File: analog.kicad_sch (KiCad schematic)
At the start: 13 parts, among them U3 AD620, U4 OPA358, U5 OPA358

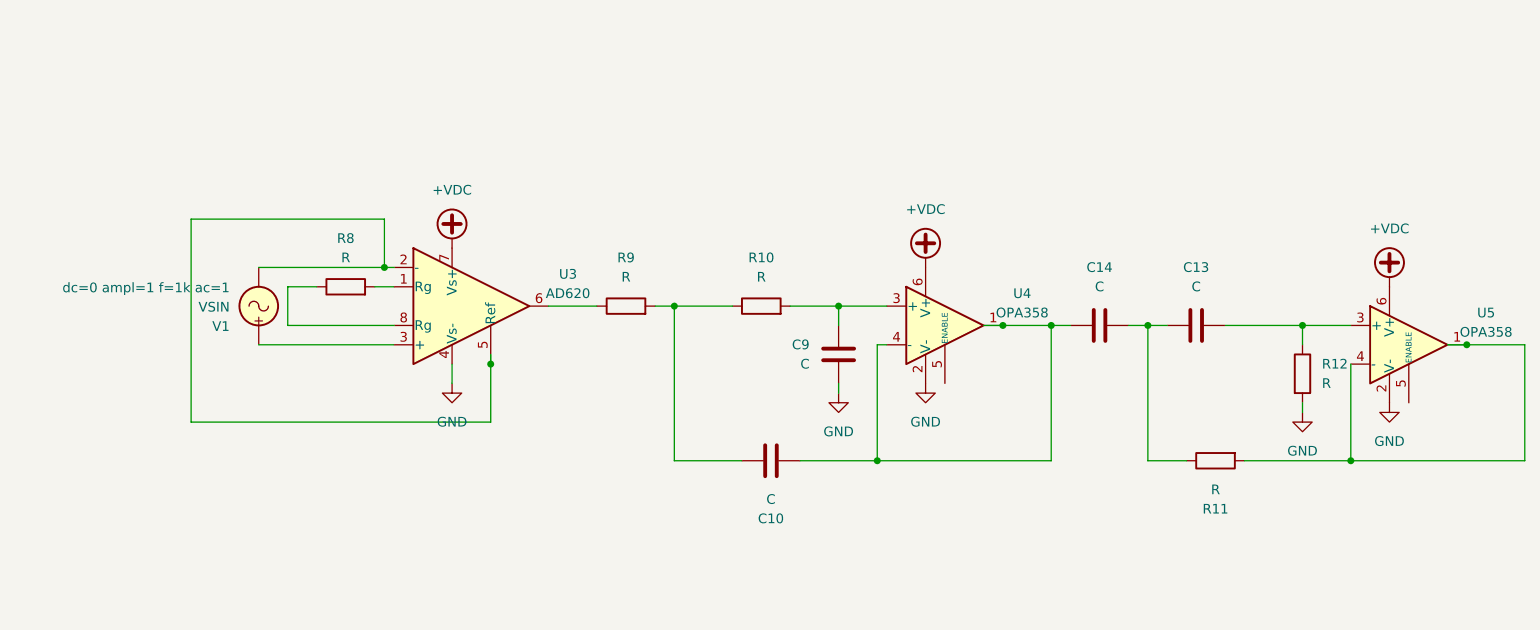
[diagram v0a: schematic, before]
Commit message: removed high pass
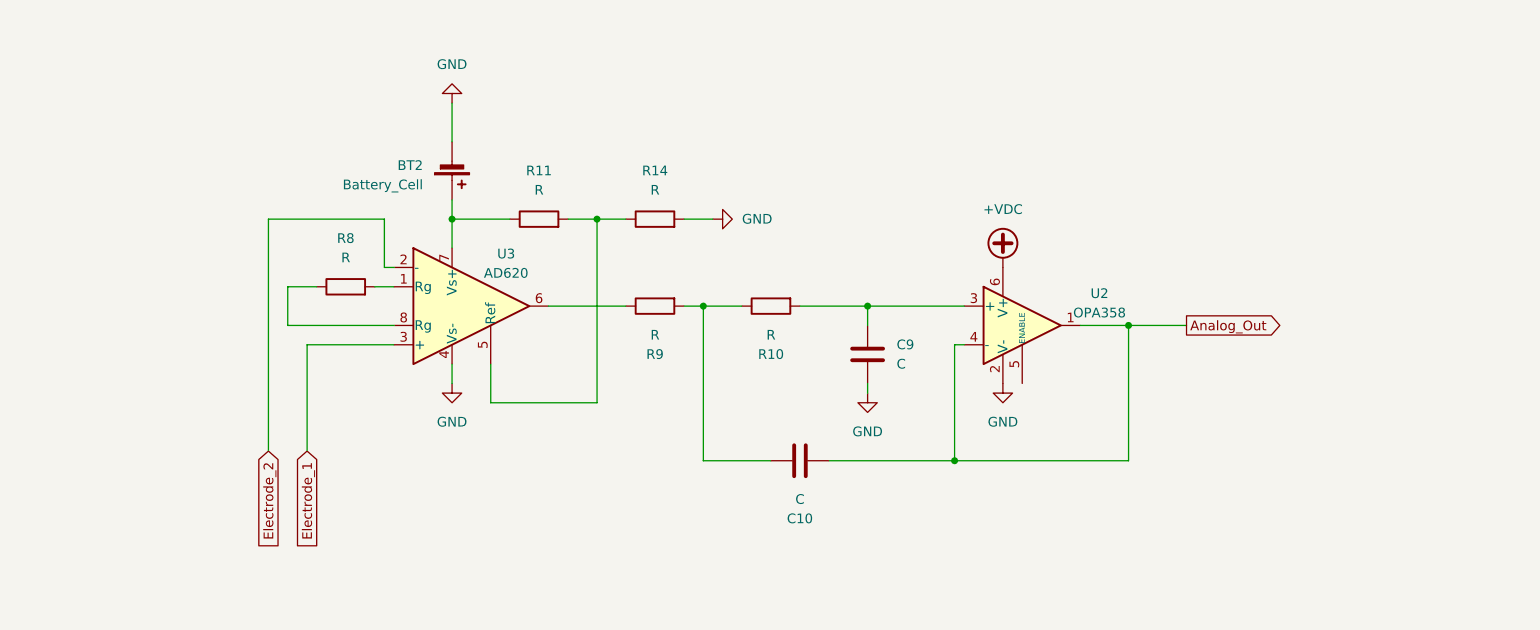
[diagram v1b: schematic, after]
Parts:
- removed C13, C14: C, symbol Device:C
- removed R12: R, symbol Device:R
- removed U4, U5: OPA358, symbol OPA358:OPA358
- removed V1: VSIN, symbol Simulation_SPICE:VSIN
- added BT2: Battery_Cell, symbol Device:Battery_Cell
- added R14: R, symbol Device:R
- added U2: OPA358, opa358-local:DCK6-M, symbol OPA358:OPA358
- U3: footprint (none) -> ad620-local:R_8_ADI-M
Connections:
- net +VDC: now also U2.6 (V+); no longer U3.7 (Vs+)
- net GND: now also BT2.2 (-), R14.2, U2.2 (V-)
- net at R11.1: now also U3.7 (Vs+), BT2.1 (+)
- net at C9.1, R10.2: now also U2.3 (+)
- net at R11.2: now also U3.5 (Ref), R14.1
- net Analog_Out: now reaches C10.2
- net Analog_Out: now also U2.1, U2.4 (-)
- net Electrode_2: now reaches U3.2 (-)
- net Electrode_2: no longer U3.5 (Ref)
- net Electrode_1: now reaches U3.3 (+)
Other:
- moved on the sheet: C10, C9, R10, R9

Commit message: Modified analog as per sir(Lab)
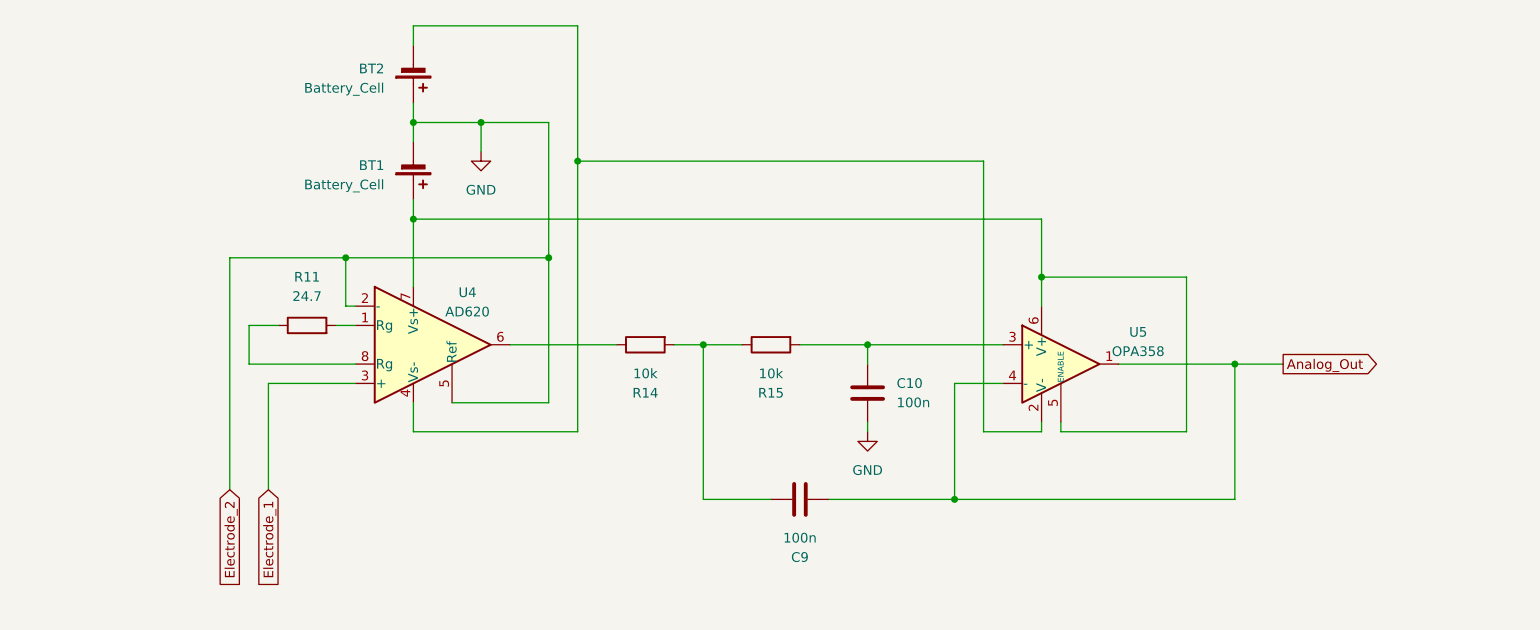
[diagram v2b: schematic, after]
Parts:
- removed R10, R8, R9: R, symbol Device:R
- removed U2: OPA358, opa358-local:DCK6-M, symbol OPA358:OPA358
- removed U3: AD620, ad620-local:R_8_ADI-M, symbol Amplifier_Instrumentation:AD620
- added BT1: Battery_Cell, symbol Device:Battery_Cell
- added R15: 10k, symbol Device:R
- added U4: AD620, ad620-local:R_8_ADI-M, symbol Amplifier_Instrumentation:AD620
- added U5: OPA358, opa358-local:DCK6-M, symbol OPA358:OPA358
- C10, C9: value C -> 100n
- R11: value R -> 24.7
- R14: value R -> 10k
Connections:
- net Analog_Out: now also C9.2, U5.1, U5.4 (-); no longer C10.2
- net Electrode_1: now also U4.3 (+)
- net GND: now also BT2.1 (+), C10.2, BT1.2 (-), U4.2 (-), U4.5 (Ref); no longer BT2.2 (-), C9.2, R14.2
- net at C9.1: now also R14.2, R15.1
- net at R11.1: now also U4.8 (Rg); no longer BT2.1 (+)
- net at R11.2: now also U4.1 (Rg); no longer R14.1
- net at C10.1: now also R15.2, U5.3 (+)
- new net: BT2.2 (-), U4.4 (Vs-), U5.2 (V-)
- new net: BT1.1 (+), U4.7 (Vs+), U5.5 (ENABLE), U5.6 (V+)
- new net: R14.1, U4.6

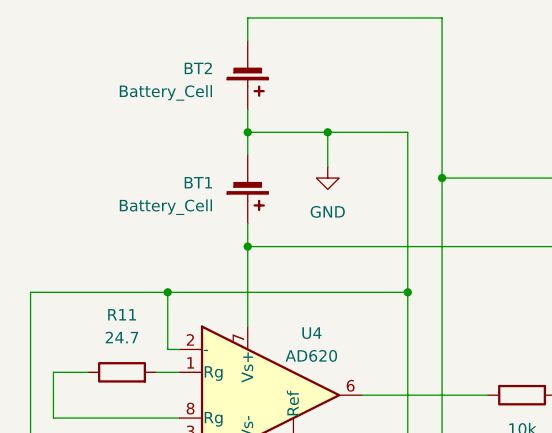
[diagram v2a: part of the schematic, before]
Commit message: Created and added Symbols for previous blackboxes
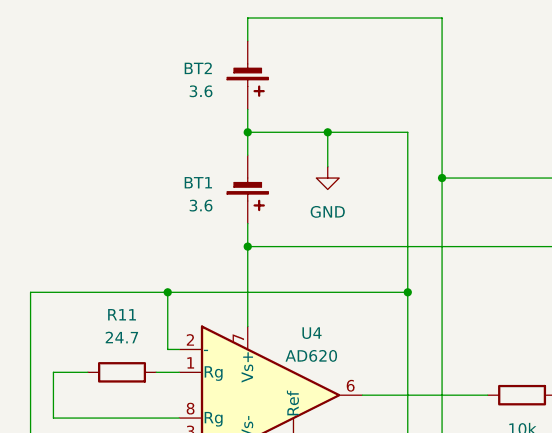
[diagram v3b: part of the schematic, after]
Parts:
- BT1, BT2: value Battery_Cell -> 3.6

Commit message: Assigned footprints for Resistors and Capacitors
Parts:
- C10, C9: footprint (none) -> Capacitor_SMD:C_0201_0603Metric
- R11, R14, R15: footprint (none) -> Resistor_SMD:R_0201_0603Metric
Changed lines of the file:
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@@
 			)
 		)
-		(property "Footprint" ""
+		(property "Footprint" "Capacitor_SMD:C_0201_0603Metric"
 			(at 150.8252 100.33 0)
 			(effects
@@
 			)
 		)
-		(property "Footprint" ""
+		(property "Footprint" "Resistor_SMD:R_0201_0603Metric"
 			(at 137.16 88.392 90)
 			(effects
@@
 			)
 		)
-		(property "Footprint" ""
+		(property "Footprint" "Resistor_SMD:R_0201_0603Metric"
 			(at 76.2 89.408 90)
 			(effects
@@
 			)
 		)
-		(property "Footprint" ""
+		(property "Footprint" "Resistor_SMD:R_0201_0603Metric"
 			(at 120.65 88.392 90)
 			(effects
@@
 			)
 		)
-		(property "Footprint" ""
+		(property "Footprint" "Capacitor_SMD:C_0201_0603Metric"
 			(at 144.78 111.4552 0)
 			(effects

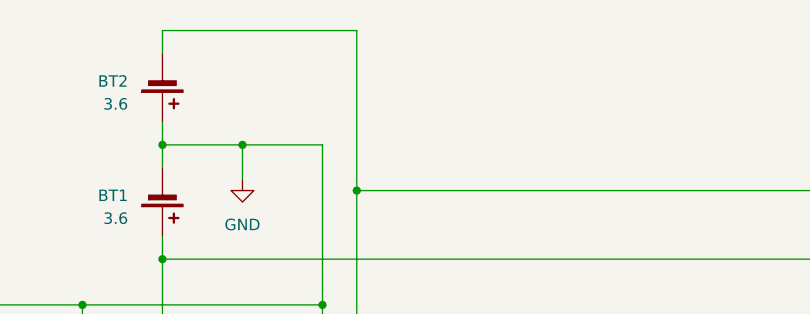
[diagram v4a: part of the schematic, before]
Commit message: Connect unused GPIO pins to Vs-
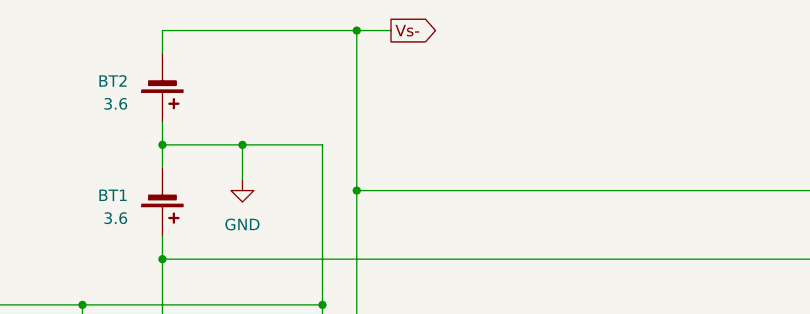
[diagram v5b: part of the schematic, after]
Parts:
- U4: footprint ad620-local:R_8_ADI-M -> ad620:R_8_ADI-M
- U5: footprint opa358-local:DCK6-M -> opa358:DCK6-M
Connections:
- net Vs-: now reaches BT2.2 (-), U4.4 (Vs-), U5.2 (V-)
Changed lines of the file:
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@@
 	(paper "A4")
+	(junction
+		(at 111.76 48.26)
+		(diameter 0)
+		(color 0 0 0 0)
+	)
 	(junction
 		(at 128.27 90.17)
@@
 		(pts
 			(xy 111.76 66.04) (xy 111.76 101.6)
+		)
+		(stroke
+			(width 0)
+			(type default)
+		)
+	)
+	(wire
+		(pts
+			(xy 111.76 48.26) (xy 115.57 48.26)
 		)
 		(stroke
@@
 		(property "Intersheetrefs" "${INTERSHEET_REFS}"
 			(at 217.9778 92.71 0)
+			(effects
+				(font
+					(size 1.27 1.27)
+				)
+				(justify left)
+				(hide yes)
+			)
+		)
+	)
+	(global_label "Vs-"
+		(shape output)
+		(at 115.57 48.26 0)
+		(fields_autoplaced yes)
+		(effects
+			(font
+				(size 1.27 1.27)
+			)
+			(justify left)
+		)
+		(property "Intersheetrefs" "${INTERSHEET_REFS}"
+			(at 122.2443 48.26 0)
 			(effects
 				(font
@@
 			)
 		)
-		(property "Footprint" "opa358-local:DCK6-M"
+		(property "Footprint" "opa358:DCK6-M"
 			(at 179.07 99.06 0)
 			(effects
@@
 			)
 		)
-		(property "Footprint" "ad620-local:R_8_ADI-M"
+		(property "Footprint" "ad620:R_8_ADI-M"
 			(at 92.71 90.17 0)
 			(effects

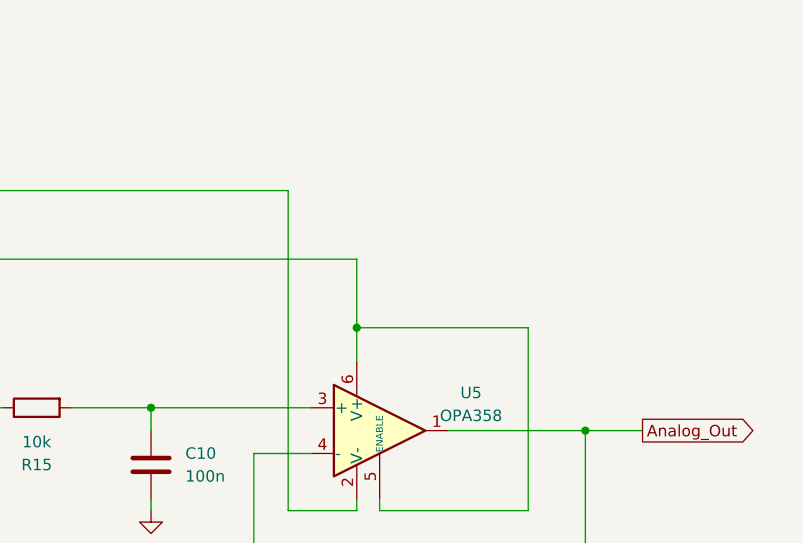
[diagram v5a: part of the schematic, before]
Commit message: Remove external oscillator, connect all GND to VS-, Fix ERC Errors.
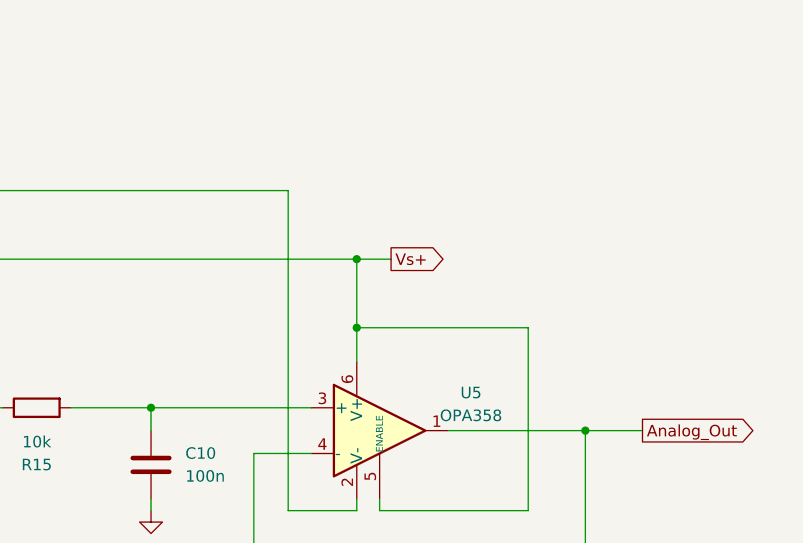
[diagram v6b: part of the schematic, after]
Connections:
- net Vs+: now reaches BT1.1 (+), U4.7 (Vs+), U5.5 (ENABLE), U5.6 (V+)
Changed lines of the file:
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@@
+	)
+	(junction
+		(at 172.72 73.66)
+		(diameter 0)
+		(color 0 0 0 0)
 	)
 	(junction
@@
 		(pts
 			(xy 90.17 97.79) (xy 90.17 101.6)
+		)
+		(stroke
+			(width 0)
+			(type default)
+		)
+	)
+	(wire
+		(pts
+			(xy 172.72 73.66) (xy 176.53 73.66)
 		)
 		(stroke
@@
 			(effects
 				(font
+					(size 1.27 1.27)
+				)
+				(justify left)
+				(hide yes)
+			)
+		)
+	)
+	(global_label "Vs+"
+		(shape output)
+		(at 176.53 73.66 0)
+		(fields_autoplaced yes)
+		(effects
+			(font
+				(size 1.27 1.27)
+			)
+			(justify left)
+		)
+		(property "Intersheetrefs" "${INTERSHEET_REFS}"
+			(at 183.2043 73.66 0)
+			(effects
+				(font
